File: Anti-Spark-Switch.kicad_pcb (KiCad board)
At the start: 2 copper layers, 63.2 x 42 mm, 16 parts, among them P1 Pad_Conn, P2 Pad_Conn, P3 Screw_Terminal, P4 Screw_Terminal, P5 Pad_Conn, P6 Pad_Conn, P7 CONN_01X02, Q1 IRFS7530, Q2 IRFS7530, Q3 IRFS7530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

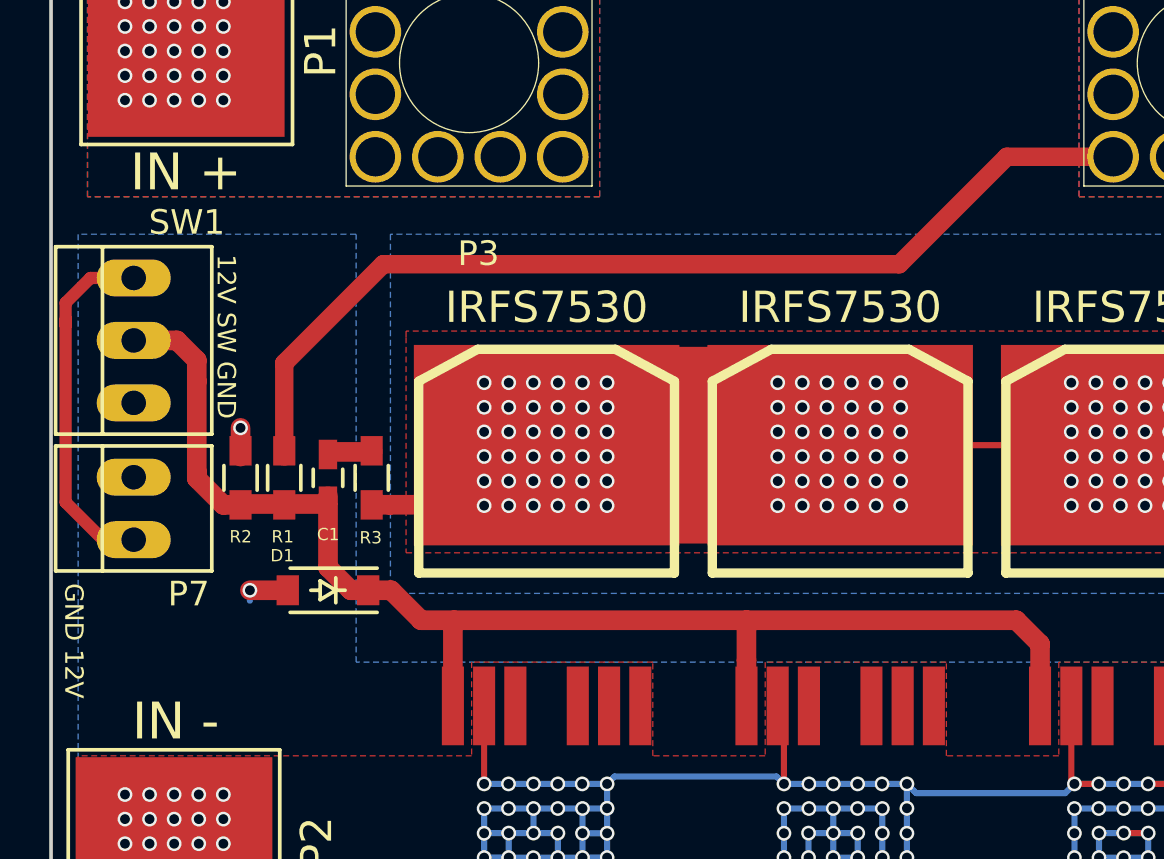
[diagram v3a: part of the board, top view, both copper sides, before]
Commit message: Fixed short through LED issue
may still need some tweaking
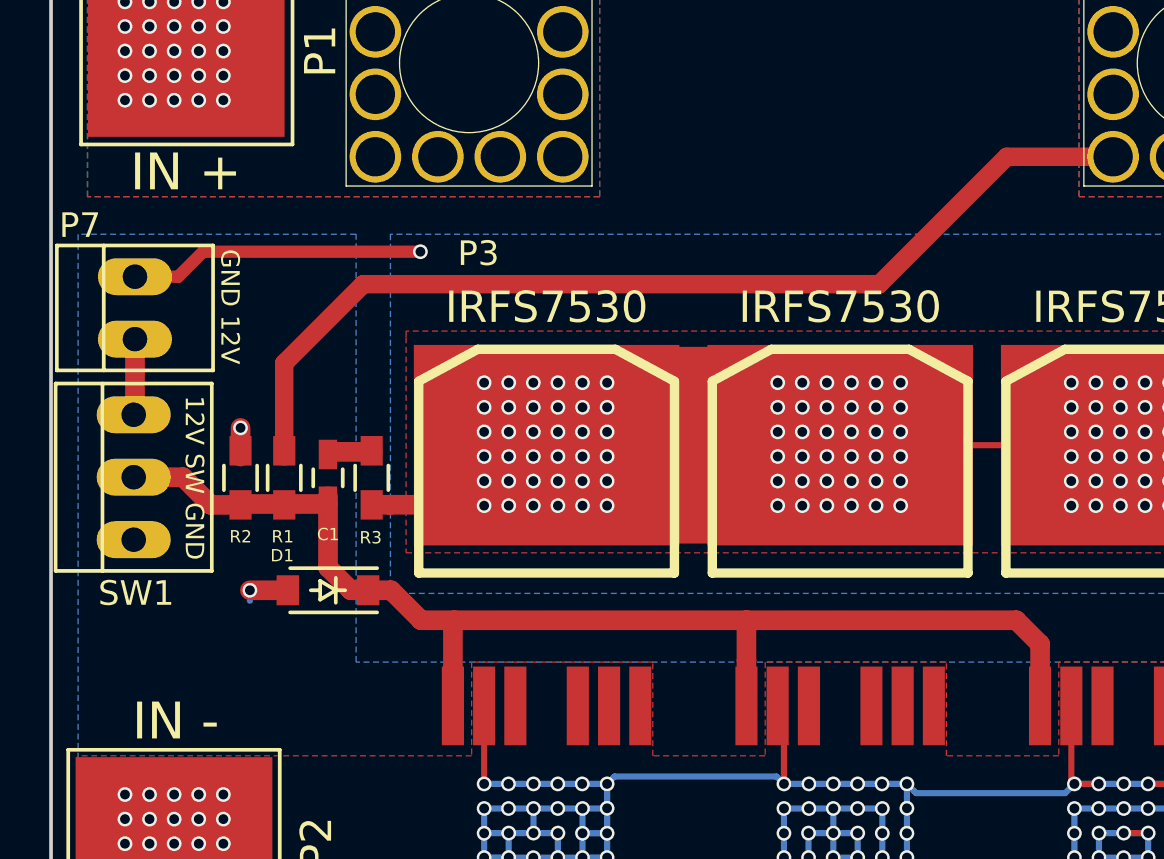
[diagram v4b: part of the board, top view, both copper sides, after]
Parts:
- moved P7 8.15 mm to (183.4, 64.0)
- moved SW1 5.56 mm to (183.4, 70.8)
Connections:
- P7 pad 2: GND -> Net-(P6-Pad1)
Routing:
- net Net-(P6-Pad1): track 104.4 -> 116.5 mm, vias 133 -> 134
- net +12V: track 14.7 -> 3.09 mm
- net Net-(C1-Pad2): track 56.1 -> 51.0 mm
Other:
- board text added: "Ver: 1.2 Date: 2/17"
- board text removed: "Ver: 1.1 Date: 9/16"
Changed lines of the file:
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@@
     (thickness 1.6)
     (drawings 14)
-    (tracks 683)
+    (tracks 678)
     (zones 0)
     (modules 16)
@@
     (mod_text_size 1 1)
     (mod_text_width 0.15)
-    (pad_size 8 7)
-    (pad_drill 0)
+    (pad_size 1.50622 3.01498)
+    (pad_drill 0.99822)
     (pad_to_mask_clearance 0.2)
     (aux_axis_origin 0 0)
@@
   )
   (module Connect:PINHEAD1-2 (layer F.Cu)
-    (at 183.3626 72.1106 90)
+    (at 183.4134 63.9572 90)
     (attr virtual)
-    (fp_text reference P7 (at -3.4798 2.2352 180) (layer F.SilkS)
+    (fp_text reference P7 (at 3.3528 -2.2352 180) (layer F.SilkS)
       (effects (font (size 1 1) (thickness 0.15)))
     )
@@
       (net 7 +12V))
     (pad 2 thru_hole oval (at 1.27 0 90) (size 1.50622 3.01498) (drill 0.99822) (layers *.Cu *.Mask)
-      (net 2 GND))
+      (net 6 "Net-(P6-Pad1)"))
   )
   (module Connect:PINHEAD1-3 (layer F.Cu)
-    (at 183.3626 65.278 90)
+    (at 183.3626 70.8406 90)
     (attr virtual)
-    (fp_text reference SW1 (at 4.8006 2.159 180) (layer F.SilkS)
+    (fp_text reference SW1 (at -4.7244 0.1016 180) (layer F.SilkS)
       (effects (font (size 1 1) (thickness 0.15)))
     )
@@
     (arrow2b (pts (xy 180.0098 45.9994) (xy 181.136304 45.412979)))
   )
-  (gr_text "GND 12V" (at 180.9242 77.4954 270) (layer F.SilkS)
+  (gr_text "GND 12V" (at 187.2742 63.9064 270) (layer F.SilkS)
     (effects (font (size 0.75 0.75) (thickness 0.1875)))
   )
-  (gr_text "Ver: 1.1\nDate: 9/16" (at 212.344 54.4322) (layer B.SilkS)
+  (gr_text "Ver: 1.2\nDate: 2/17" (at 212.344 54.4322) (layer B.SilkS)
     (effects (font (size 1.5 1.5) (thickness 0.3)) (justify mirror))
   )
@@
     (effects (font (size 1.5 1.5) (thickness 0.3)) (justify mirror))
   )
-  (gr_text "12V SW GND" (at 187.1218 65.1256 270) (layer F.SilkS)
+  (gr_text "12V SW GND" (at 185.8264 70.866 270) (layer F.SilkS)
     (effects (font (size 0.75 0.75) (thickness 0.1875)))
   )
@@
   (segment (start 221.488 83.185) (end 221.615 83.312) (width 0.25) (layer F.Cu) (net 2))
   (via (at 221.615 83.312) (size 0.6) (drill 0.4) (layers F.Cu B.Cu) (net 2))
-  (segment (start 183.3626 65.278) (end 185.12009 65.278) (width 0.8) (layer F.Cu) (net 3))
-  (segment (start 185.12009 65.278) (end 185.928 66.08591) (width 0.8) (layer F.Cu) (net 3))
-  (segment (start 185.928 66.08591) (end 185.928 66.93662) (width 0.8) (layer F.Cu) (net 3))
-  (segment (start 187.706 71.966) (end 187.006 71.966) (width 0.8) (layer F.Cu) (net 3))
-  (segment (start 187.006 71.966) (end 185.928 70.888) (width 0.8) (layer F.Cu) (net 3))
-  (segment (start 185.928 70.888) (end 185.928 70.612) (width 0.8) (layer F.Cu) (net 3))
-  (segment (start 185.928 70.612) (end 185.928 66.93662) (width 0.8) (layer F.Cu) (net 3))
+  (segment (start 186.4946 71.966) (end 185.3692 70.8406) (width 0.8) (layer F.Cu) (net 3))
+  (segment (start 185.3692 70.8406) (end 183.3626 70.8406) (width 0.8) (layer F.Cu) (net 3))
+  (segment (start 187.706 71.966) (end 186.4946 71.966) (width 0.8) (layer F.Cu) (net 3))
   (segment (start 219.2528 76.6572) (end 208.28 76.6572) (width 0.8) (layer F.Cu) (net 3))
   (segment (start 208.28 76.6572) (end 196.3928 76.6572) (width 0.8) (layer F.Cu) (net 3))
@@
   (segment (start 191.24 71.93) (end 189.462 71.93) (width 0.8) (layer F.Cu) (net 3))
   (segment (start 193.078 69.81) (end 191.3 69.81) (width 0.8) (layer F.Cu) (net 4))
-  (segment (start 193.51 62.18) (end 189.484 66.206) (width 0.75) (layer F.Cu) (net 5))
+  (segment (start 223.19 57.81) (end 218.865787 57.81) (width 0.75) (layer F.Cu) (net 5))
+  (segment (start 218.865787 57.81) (end 213.683787 62.992) (width 0.75) (layer F.Cu) (net 5))
+  (segment (start 213.683787 62.992) (end 192.698 62.992) (width 0.75) (layer F.Cu) (net 5))
+  (segment (start 192.698 62.992) (end 189.484 66.206) (width 0.75) (layer F.Cu) (net 5))
   (segment (start 189.484 66.206) (end 189.484 70) (width 0.75) (layer F.Cu) (net 5))
-  (segment (start 214.495787 62.18) (end 193.51 62.18) (width 0.75) (layer F.Cu) (net 5))
-  (segment (start 223.19 57.81) (end 218.865787 57.81) (width 0.75) (layer F.Cu) (net 5))
-  (segment (start 218.865787 57.81) (end 214.495787 62.18) (width 0.75) (layer F.Cu) (net 5))
   (segment (start 238.0074 55.4858) (end 237.0074 55.4858) (width 0.25) (layer F.Cu) (net 5))
   (segment (start 239.0074 55.4858) (end 238.0074 55.4858) (width 0.25) (layer F.Cu) (net 5))
@@
   (via (at 238.0074 51.4858) (size 0.6) (drill 0.4) (layers F.Cu B.Cu) (net 5))
   (via (at 237.0074 51.4858) (size 0.6) (drill 0.4) (layers F.Cu B.Cu) (net 5))
+  (segment (start 183.4134 62.6872) (end 185.17089 62.6872) (width 0.5) (layer F.Cu) (net 6))
+  (segment (start 185.17089 62.6872) (end 186.18689 61.6712) (width 0.5) (layer F.Cu) (net 6))
+  (segment (start 186.18689 61.6712) (end 195.0212 61.6712) (width 0.5) (layer F.Cu) (net 6))
+  (via (at 195.0212 61.6712) (size 0.6) (drill 0.4) (layers F.Cu B.Cu) (net 6))
   (segment (start 241.0074 86.7184) (end 241.0074 87.7184) (width 0.25) (layer F.Cu) (net 6))
   (segment (start 240.0074 86.7184) (end 241.0074 86.7184) (width 0.25) (layer F.Cu) (net 6))
@@
   (segment (start 193.1 71.96) (end 193.8 71.96) (width 0.8) (layer F.Cu) (net 6))
   (segment (start 195.81842 69.53758) (end 200.152 69.53758) (width 0.25) (layer F.Cu) (net 6))
-  (segment (start 180.594 71.86149) (end 180.594 64.66) (width 0.5) (layer F.Cu) (net 7))
-  (segment (start 180.594 64.66) (end 180.594 64.39662) (width 0.5) (layer F.Cu) (net 7))
-  (segment (start 183.3626 62.738) (end 181.60511 62.738) (width 0.5) (layer F.Cu) (net 7))
-  (segment (start 181.60511 62.738) (end 180.594 63.74911) (width 0.5) (layer F.Cu) (net 7))
-  (segment (start 180.594 63.74911) (end 180.594 64.66) (width 0.5) (layer F.Cu) (net 7))
-  (segment (start 183.134 73.406) (end 182.13851 73.406) (width 0.25) (layer F.Cu) (net 7))
-  (segment (start 182.13851 73.406) (end 180.594 71.86149) (width 0.5) (layer F.Cu) (net 7))
+  (segment (start 183.4134 65.2272) (end 183.4134 68.2498) (width 0.8) (layer F.Cu) (net 7))
+  (segment (start 183.4134 68.2498) (end 183.3626 68.3006) (width 0.25) (layer F.Cu) (net 7))
   (zone (net 2) (net_name GND) (layer F.Cu) (hatch edge 0.508)
     (connect_pads yes (clearance 0.508))

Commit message: updated the PCB per new schematic changes and general improvements
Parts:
- added R4: 16.5K, Resistors_SMD:R_1206, F.Cu at (126.8, 92.6)
- added R5: 16.5K, Resistors_SMD:R_1206, F.Cu at (124.5, 92.6)
- C1: footprint Capacitors_SMD:C_0603_HandSoldering -> Capacitors_SMD:C_0603
- P3, P4: footprint Spark_Parts:M5_Screw_Terminal_12_pin -> sparkparts:M5_Screw_Terminal_12_pin
- R1, R2, R3: footprint Resistors_SMD:R_0603_HandSoldering -> Resistors_SMD:R_0603
- moved C1 72.6 mm to (124.6, 99.5), turned to 180 degrees
- moved R3 71.7 mm to (127.3, 99.5), turned to 180 degrees
- moved D1 71.1 mm to (125.4, 102.2), turned to 0 degrees
- moved P3 70.8 mm to (132.3, 82.8)
- moved P4 70.8 mm to (162.3, 82.8)
- moved LED 70.5 mm to (119.1, 92.7)
- moved P1 70.5 mm to (121.2, 82.3)
- moved P2 70.5 mm to (120.7, 114.5)
- moved P5 70.5 mm to (174.2, 82.3)
- moved P6 70.5 mm to (174.3, 114.4)
- moved Q2 70.5 mm to (147.8, 104.2)
- moved Q3 70.5 mm to (159.7, 104.2)
- moved SWITCH 70.5 mm to (119.1, 99.6)
- moved Q1 70.5 mm to (135.8, 104.2)
- moved R1 70.2 mm to (124.6, 97.7), turned to 180 degrees
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- renumbered P7 to LED, SW1 to SWITCH
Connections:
- net +12V renamed Net-(P7-Pad1)
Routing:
- net Net-(P7-Pad1): track 3.09 -> 10.8 mm
- net Net-(P4-Pad1): track 67.8 -> 73.7 mm
- net Net-(C1-Pad2): track 51.0 -> 55.1 mm
- net Net-(P6-Pad1): track 116.5 -> 120.5 mm
- net Net-(C1-Pad1): track 1.78 -> 1.25 mm
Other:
- net class Default: clearance 0.2 -> 0
- rule trace_clearance: 0.2 -> 0
- board text added: "AntiSpark"
- board text added: "Ver: 1.3 Date: 4/21/18"
- board text removed: "GiS AntiSpark"
- board text removed: "Ver: 1.2 Date: 2/17"
